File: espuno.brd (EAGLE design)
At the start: 68.6 x 53.3 mm, 34 parts, among them T1 FDN340P, U1 ADS1115IDGST, U2 NCP1117ST50T3G, U3 LP2985-33DBVR, U4 FT232R, U5 LMV358IDGKR, X1 POWERSUPPLY_DC21MMX

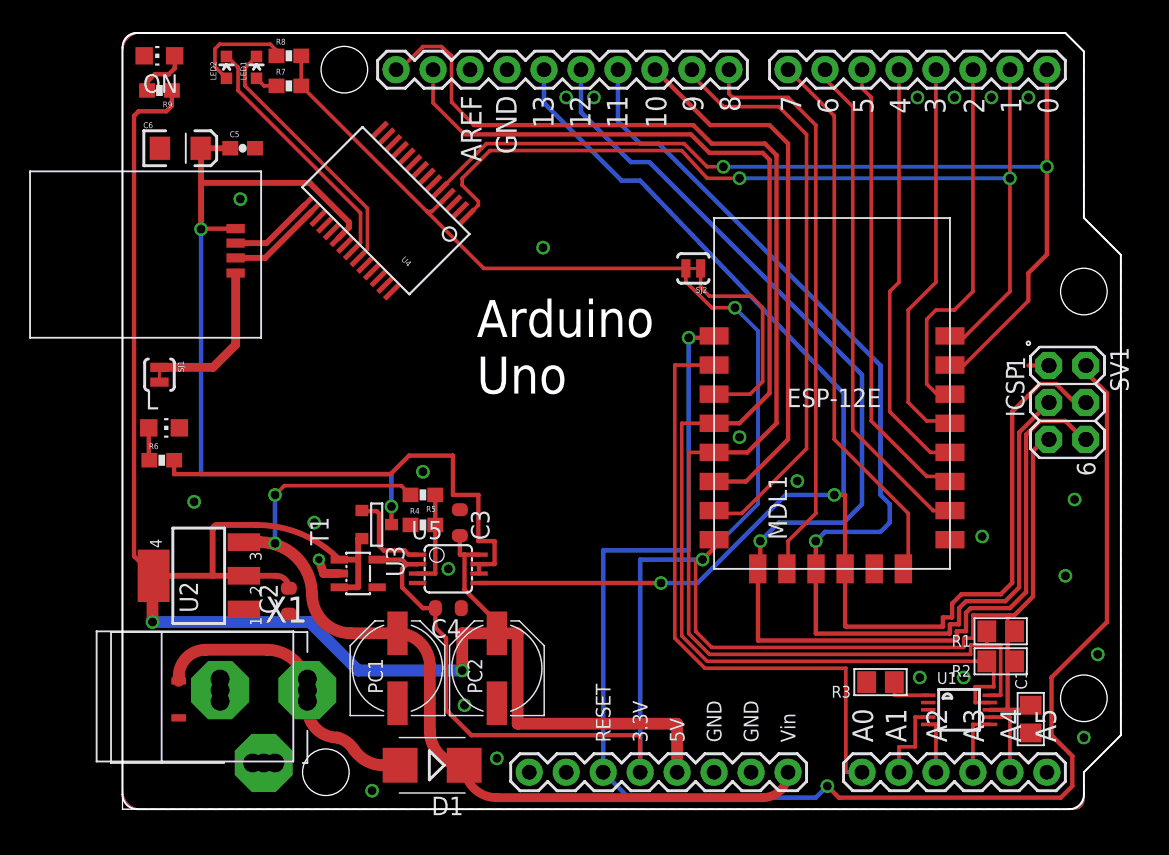
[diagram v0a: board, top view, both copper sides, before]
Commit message: Added LIPO parts, use more 0805 resistors/caps and 1206 LEDs instead of f&cking 0402s
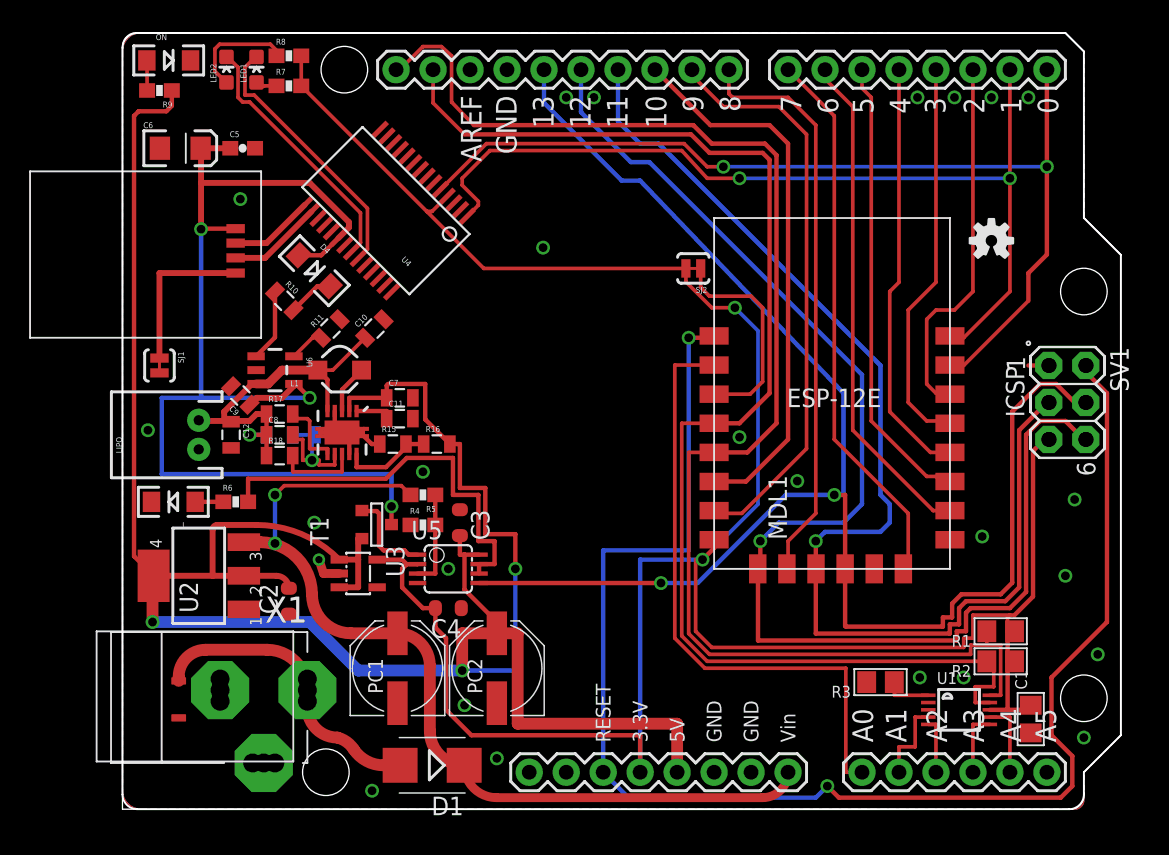
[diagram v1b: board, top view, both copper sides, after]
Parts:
- added C10, C9: 4.7uF, SparkFun-Capacitors:0805
- added C11, C8: 0.1uF, SparkFun-Capacitors:0805
- added C12: 10uF, SparkFun-Capacitors:0805
- added C7: 22uF, SparkFun-Capacitors:0805
- added D4: CHARGING, SparkFun-LED:LED-1206
- added L1: 4.7uH, 1.2A, SparkFun:CDRH2D09
- added LIPO: (no value), SparkFun-Connectors:JST-2-PTH
- added R10: 470, SparkFun-Resistors:0805
- added R11: 2k, SparkFun-Resistors:0805
- added R12, R16: 2M, SparkFun-Resistors:0805
- added R13, R15: 220k, SparkFun-Resistors:0805
- added R17, R18: 10k, SparkFun-Resistors:0805
- added U$1: OSHW-LOGOS, SparkFun:OSHW-LOGO-S
- added U6: MCP73831, SparkFun:SOT23-5
- added U7: TPS61200, SparkFun:QFN-10_PAD
- L, ON: device led:CHIP-LED0805 -> SparkFun-LED:LED-1206
- LED1: value Red -> RED
- LED2: value Green -> GREEN
- moved R6 5.83 mm to (7.78, 21.1)
- moved L 5.12 mm to (3.49, 21.1), turned to 180 degrees
- moved ON 0.71 mm to (3.17, 51.4), turned to 0 degrees
- moved SJ1 0.64 mm to (2.54, 30.5)
- moved LED1 0.16 mm to (9.21, 50.8)
- moved LED2 0.16 mm to (7.14, 50.8)
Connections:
- new net EN: R17.2, U7.6
- new net FB: R15.2, R16.1, U7.10
- new net N$11: R11.1, U6.5
- new net N$14: R10.1, U6.1
- new net N$5: L1.P$1, U7.3
- new net N$6: C11.1, U7.1
- new net N$8: D4.C, R10.2
- new net PS: R18.2, U7.8
- new net UVLO: C8.2, R12.1, R13.2, U7.7
- new net VBATT: C10.1, C12.1, C8.1, L1.P$2, LIPO.2, R12.2, R17.1, R18.1, U6.3, U7.5
- net 5V: now also C7.1, R16.2, U7.2
- net GND: now also C10.2, C11.2, C12.2, C7.2, C9.2, LIPO.1, R11.2, R13.1, R15.1, U6.2, U7.11, U7.12, U7.13, U7.14, U7.15, U7.4, U7.9
- net USBVCC: now also C9.1, D4.A, U6.4
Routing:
- net 5V: track 126.1 -> 161.6 mm, vias 2 -> 3
- net VBATT: track 0.00 -> 26.4 mm, vias 0 -> 1
- net USBVCC: track 56.1 -> 77.3 mm, vias 2 -> 3
- net UVLO: track 0.00 -> 8.79 mm, vias 0 -> 1
- net GND: track 3.51 -> 11.9 mm
- net FB: track 0.00 -> 6.30 mm
- net PS: track 0.00 -> 5.72 mm
- net N$14: track 0.00 -> 4.99 mm
- net EN: track 0.00 -> 4.85 mm
- net L13: track 32.7 -> 28.1 mm
- net N$5: track 0.00 -> 3.37 mm
- net N$8: track 0.00 -> 3.17 mm
- net N$6: track 0.00 -> 2.59 mm
- net N$11: track 0.00 -> 2.40 mm
- net N$1: track 3.73 -> 2.07 mm

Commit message: Fixing layout of labels, adding ESPUNO text, slight layout tweaks to make slightly more pleasing.
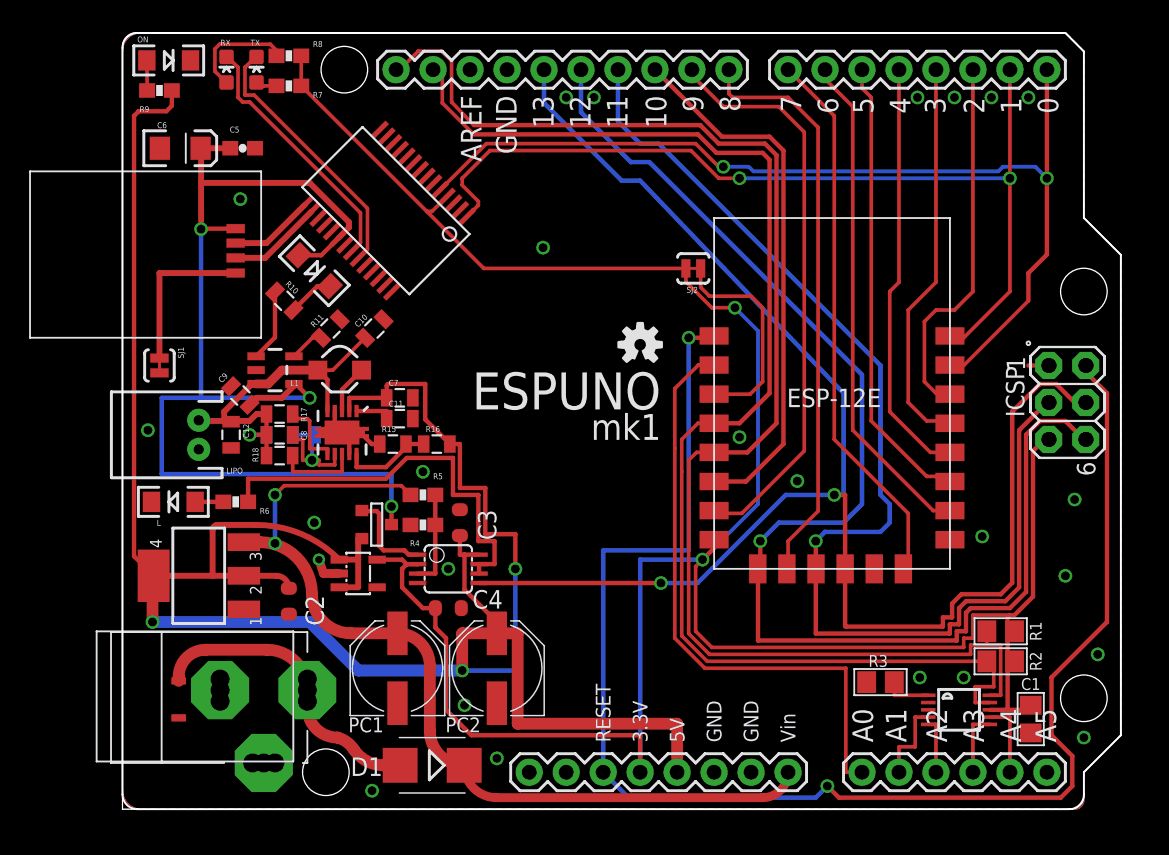
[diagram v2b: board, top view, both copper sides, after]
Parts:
- moved U$1 25.2 mm to (35.6, 31.9)
- renumbered LED1 to TX, LED2 to RX
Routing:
- net SDA: track 91.8 -> 90.8 mm
- net ADC: track 42.3 -> 41.4 mm
- net SCL: track 97.3 -> 96.5 mm
- net 10: track 37.8 -> 37.1 mm
- net RX: track 67.3 -> 67.9 mm
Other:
- board text added: "ESPUNO"
- board text added: "mk1"

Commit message: Espuno Mk2, with bigass 1206's for errything
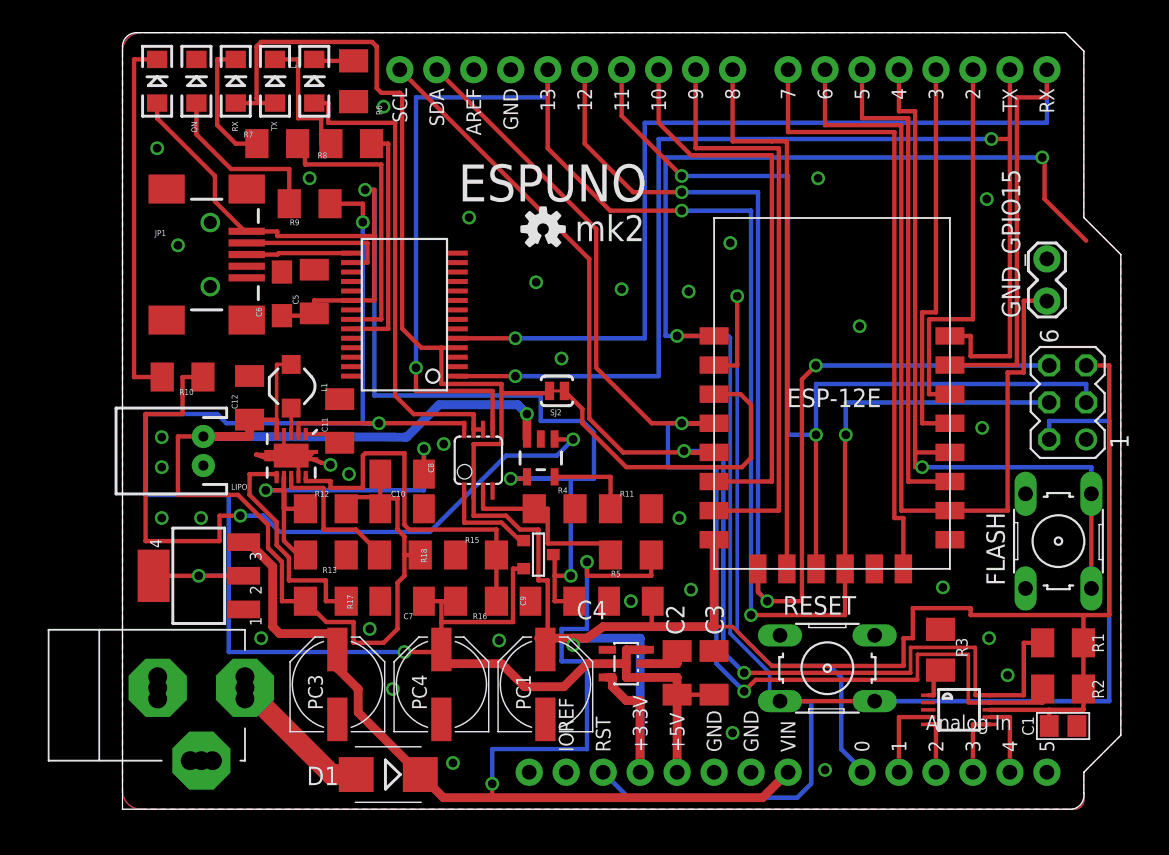
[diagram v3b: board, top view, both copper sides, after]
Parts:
- removed PC2: 47u, rcl:PANASONIC_D
- removed PCB1: ARDUINO_UNO, E14_Arduino_revB:ARDUINO_UNO
- removed SJ1: JUMPER-PAD-2-NC_BY_TRACE, SparkFun-Passives:PAD-JUMPER-2-NC_BY_TRACE_YES_SILK
- added FLASH, RESET: (no value), switch-omron:B3F-10XX
- added GND_GPIO15: (no value), SparkFun-Retired:1X02_LOCK
- added J1: ARDUINO_R3_SHIELD, SparkFun-Boards:UNO_R3_SHIELD
- added JP1: USB-SMD-NS, SparkFun-Connectors:USB-MINIB-NOSTOP
- added PC3, PC4: 47u, rcl:PANASONIC_D
- C10, C11, C12, C7, C8, C9: device SparkFun-Capacitors:0805 -> rcl:C1206K
- C2, C3, C4: device SmartPrj:C0603-ROUND -> rcl:C1206K
- C5: device SparkFun-Capacitors:0603-CAP -> rcl:C1206K
- C6: device SparkFun-Capacitors:EIA3216 -> rcl:SMC_A
- R1, R2, R3: device microbuilder:0805 -> rcl:M1206
- R10, R11, R12, R13, R15, R16, R17, R18: device SparkFun-Resistors:0805 -> rcl:M1206
- R4, R5, R6, R7, R8, R9: device SparkFun-Resistors:0603-RES -> rcl:M1206
- RX, TX: device SparkFun-LED:LED-0603 -> SparkFun-LED:LED-1206
- moved L 30.5 mm to (13.2, 50.0), turned to 90 degrees
- moved R6 30.0 mm to (15.9, 50.0), turned to 90 degrees
- moved C2 29.6 mm to (40.6, 9.37), turned to 270 degrees
- moved C9 25.7 mm to (29.5, 14.3), turned to 180 degrees
- moved R11 24.1 mm to (34.9, 20.6), turned to 0 degrees
- moved U3 19.4 mm to (34.6, 10.0), turned to 90 degrees
- moved U6 19.2 mm to (28.7, 24.1), turned to 180 degrees
- moved C3 18.1 mm to (38.1, 9.37)
- moved D4 16.9 mm to (2.38, 50.0), turned to 90 degrees
- moved R5 14.9 mm to (34.9, 17.5), turned to 0 degrees
- moved C7 14.0 mm to (19.2, 14.3), turned to 180 degrees
- moved R17 13.2 mm to (14.0, 14.3)
- moved R9 12.9 mm to (12.9, 41.6)
- moved SJ2 12.6 mm to (29.8, 28.7)
- moved C4 12.6 mm to (34.9, 14.3), turned to 0 degrees
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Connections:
- removed net N$10: PCB1.<USB>GND, SJ1.1
- removed net RXLED: RX.C, U4.22
- removed net TXLED: TX.C, U4.23
- new net AIN4: J1.A5
- new net N$7: R7.1, U4.22
- new net N$9: R8.1, U4.23
- net 10: now also J1.D10; no longer PCB1.10
- net 11/MOSI: now also J1.D11; no longer PCB1.11
- net 12/MISO: now also J1.D12; no longer PCB1.12
- net 13/SCLK: now also J1.D13; no longer PCB1.13
- net 2: now also J1.D2; no longer PCB1.2
- net 3: now also J1.D3; no longer PCB1.3
- net 3.3V: now also J1.3.3V, PC1.+, RX.A, TX.A; no longer PCB1.3.3V, R7.2, R8.2
- net 4: now also FLASH.3, FLASH.4, J1.D4; no longer PCB1.4
- net 5: now also J1.D5; no longer PCB1.5
- net 5V: now also J1.5V, PC4.+; no longer PC2.+, PCB1.5V
- net 6: now also GND_GPIO15.1, J1.D6; no longer PCB1.6
- net 7: now also J1.D7; no longer PCB1.7
- net 8: now also J1.D8; no longer PCB1.8
- net 9: now also J1.D9; no longer PCB1.9
- net ADC: now also J1.A0; no longer PCB1.A0
- net AIN0: now also J1.A1; no longer PCB1.A1
- net AIN1: now also J1.A2; no longer PCB1.A2
- net AIN2: now also J1.A3; no longer PCB1.A3
- net AIN3: now also J1.A4; no longer PCB1.A4
- net GND: now also C6.-, FLASH.1, FLASH.2, GND_GPIO15.2, J1.GND@0, J1.GND@1, J1.GND@2, JP1.GND, PC3.-, PC4.-, R6.1, RESET.1, RESET.2; no longer C6.C, L.C, PC2.-, PCB1.<PWR>-V, PCB1.A5, PCB1.GND, PCB1.GND., PCB1.GND.., SJ1.2
- net L13: now also L.A; no longer R6.2
- net N$2: now also L.C, R6.2; no longer L.A, R6.1
- net N$3: now also R7.2, RX.C; no longer R7.1, TX.A
- net N$4: now also R8.2, TX.C; no longer R8.1, RX.A
- net PWRIN: no longer PCB1.<PWR>+V
- net RESET: now also J1.RES, RESET.3, RESET.4; no longer PCB1.RESET
- net RX: now also J1.RX; no longer PCB1.0
- net SCL: now also J1.SCL; no longer PCB1.SCL
- net SDA: now also J1.SDA; no longer PCB1.SDA
- net TX: now also J1.TX; no longer PCB1.1
- net USBVCC: now also C6.+, JP1.VBUS; no longer C6.A, PCB1.<USB>+V
- net USB_D+: now also JP1.D+; no longer PCB1.<USB>D+
- net USB_D-: now also JP1.D-; no longer PCB1.<USB>D-
- net VIN: now also J1.VIN, PC3.+; no longer PC1.+, PCB1.VIN
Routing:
- net VBATT: track 26.4 -> 84.1 mm
- net RESET: track 103.2 -> 149.0 mm
- net N$14: track 4.99 -> 50.7 mm, vias 0 -> 2
- net 6: track 34.5 -> 60.0 mm
- net 5V: track 161.6 -> 138.0 mm, vias 3 -> 4
- net 4: track 29.1 -> 51.2 mm, vias 0 -> 1
- net N$8: track 3.17 -> 25.3 mm
- net 3.3V: track 165.6 -> 185.6 mm, vias 2 -> 1
- net N$7: track 0.00 -> 19.9 mm
- net VIN: track 63.4 -> 83.3 mm
- net FB: track 6.30 -> 26.0 mm
- net UVLO: track 8.79 -> 28.1 mm, vias 1 -> 2
- net TXLED: track 18.3 -> 0.00 mm
- net RX: track 67.9 -> 85.9 mm, vias 2 -> 1
- net RXLED: track 17.8 -> 0.00 mm
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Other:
- board text added: "mk2"
- board text removed: "mk1"

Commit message: Mk2 revision complete. Tidied schematics and board. Added pullups.
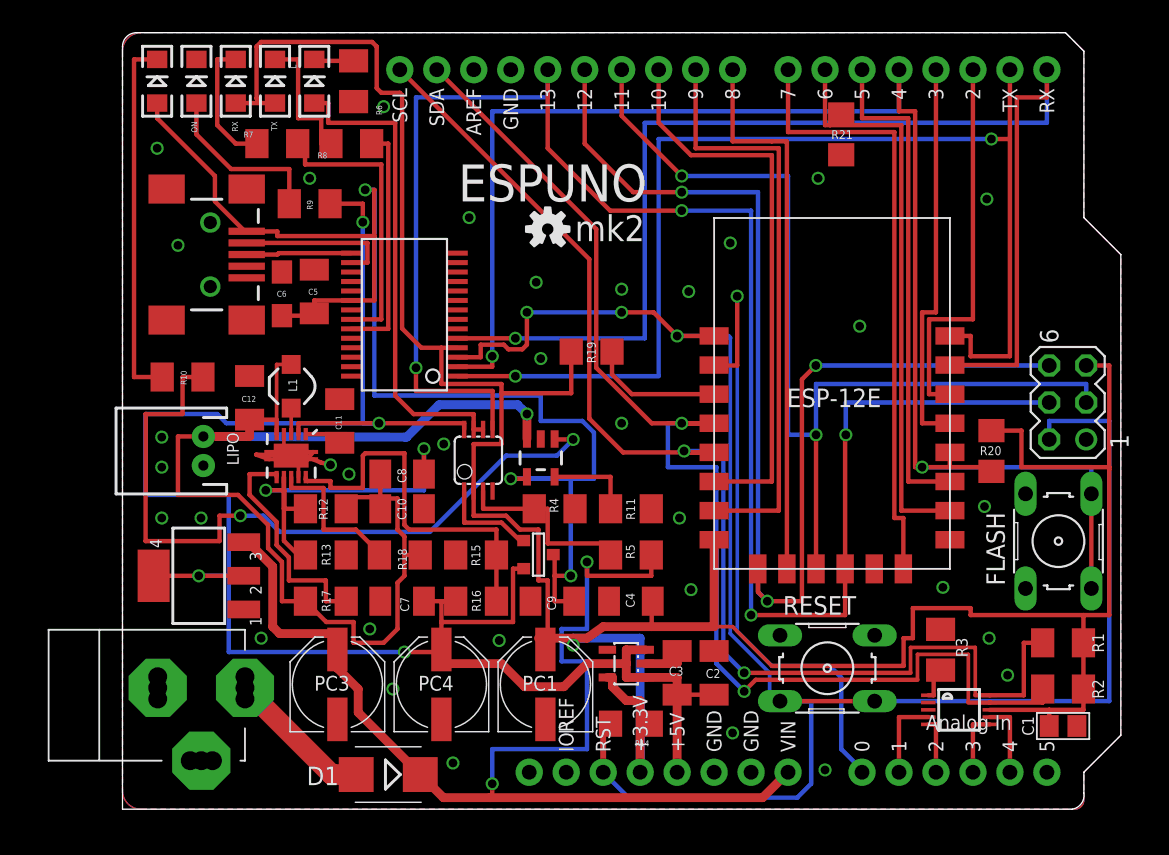
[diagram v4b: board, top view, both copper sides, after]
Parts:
- removed GND_GPIO15: (no value), SparkFun-Retired:1X02_LOCK
- removed SJ2: JUMPER-PAD-2-NC_BY_TRACE, SparkFun-Passives:PAD-JUMPER-2-NC_BY_TRACE_YES_SILK
- removed U$1: OSHW-LOGOS, SparkFun:OSHW-LOGO-S
- added FRAME1, FRAME2: (no value), SparkFun-Aesthetics:DUMMY
- added LOGO1: OSHW-LOGOS, SparkFun-Aesthetics:OSHW-LOGO-S
- added R14, R19, R20, R21: 10k, SparkFun-Resistors:1206
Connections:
- net 10 renamed 10/GPIO12
- net 2 renamed 2/GPIO5
- net 3 renamed 3/GPIO4
- net 5 renamed 5/GPIO2
- net 7 renamed 7/GPIO10
- net 8 renamed 8/GPIO9
- net 9 renamed 9/GPIO13
- net SCL renamed SCL/GPIO14
- net SDA renamed SDA/GPIO16
- removed net 4: FLASH.3, FLASH.4, J1.D4, MDL1.12
- removed net 6: GND_GPIO15.1, J1.D6, MDL1.10
- removed net DTR: U4.2
- removed net RTS: U4.3
- new net 4/GPIO0: FLASH.3, FLASH.4, J1.D4, MDL1.12, R20.2, U4.2
- new net 6/GPIO15: J1.D6, MDL1.10, R21.2
- net 3.3V: now also R14.1, R19.1, R20.1; no longer SJ2.2
- net CH_PD: now also R19.2; no longer SJ2.1
- net GND: now also R21.1; no longer GND_GPIO15.2
- net RESET: now also R14.2, U4.3
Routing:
- net 4/GPIO0: track 0.00 -> 105.6 mm, vias 0 -> 2
- net 6: track 60.0 -> 0.00 mm
- net 4: track 51.2 -> 0.00 mm, vias 1 -> 0
- net 6/GPIO15: track 0.00 -> 40.0 mm
- net RESET: track 149.0 -> 126.2 mm, vias 2 -> 3
- net 3.3V: track 185.6 -> 201.3 mm
- net CH_PD: track 22.6 -> 9.14 mm
